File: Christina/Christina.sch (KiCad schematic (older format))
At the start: 20 parts, among them K1 FINDER-32.21-x300, M1 Motor_DC, M2 Motor_DC, M3 Motor_DC, Q1 BD139, SW1 SW_Push, SW2 SW_Push, U1 74LS386, U2 L7805

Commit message: Braking PCB Rev1
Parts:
- C1, C2: footprint (none) -> Capacitors_SMD:C_0805_HandSoldering
- D1, D2: footprint LEDs:LED_0603_HandSoldering -> TerminalBlock:TerminalBlock_bornier-2_P5.08mm
- K1: footprint Relays_THT:Relay_SPST_Finder_32.21-x300 -> .pretty:SPSTRELAYPANASONIC
- M1, M2, M3, SW1, SW2: footprint TerminalBlocks_Phoenix:TerminalBlock_Phoenix_MKDS1.5-2pol -> TerminalBlock:TerminalBlock_bornier-2_P5.08mm
- Q1: footprint TO_SOT_Packages_THT:TO-126_Vertical -> TO_SOT_Packages_THT:TO-126_Horizontal
- R1, R2, R3, R4, R5, R6, R7: footprint (none) -> Resistors_SMD:R_0805_HandSoldering
- U1: footprint (none) -> .pretty:XORGATE
- U2: footprint (none) -> TO_SOT_Packages_THT:TO-126_Horizontal
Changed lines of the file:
@@
 LIBS:contrib
 LIBS:valves
+LIBS:Christina-cache
 EELAYER 25 0
 EELAYER END
@@
 F 0 "M1" H 2800 2450 50  0000 L CNN
 F 1 "Motor_DC" H 2800 2150 50  0000 L TNN
-F 2 "TerminalBlocks_Phoenix:TerminalBlock_Phoenix_MKDS1.5-2pol" H 2700 2260 50  0001 C CNN
+F 2 "TerminalBlock:TerminalBlock_bornier-2_P5.08mm" H 2700 2260 50  0001 C CNN
 F 3 "" H 2700 2260 50  0001 C CNN
 	1    2700 2350
@@
 F 0 "M2" H 5100 2450 50  0000 L CNN
 F 1 "Motor_DC" H 5100 2150 50  0000 L TNN
-F 2 "TerminalBlocks_Phoenix:TerminalBlock_Phoenix_MKDS1.5-2pol" H 5000 2260 50  0001 C CNN
+F 2 "TerminalBlock:TerminalBlock_bornier-2_P5.08mm" H 5000 2260 50  0001 C CNN
 F 3 "" H 5000 2260 50  0001 C CNN
 	1    5000 2350
@@
 F 0 "SW1" H 3350 1900 50  0000 L CNN
 F 1 "SW_Push" H 3300 1740 50  0000 C CNN
-F 2 "TerminalBlocks_Phoenix:TerminalBlock_Phoenix_MKDS1.5-2pol" H 3300 2000 50  0001 C CNN
+F 2 "TerminalBlock:TerminalBlock_bornier-2_P5.08mm" H 3300 2000 50  0001 C CNN
 F 3 "" H 3300 2000 50  0001 C CNN
 	1    3300 1800
@@
 F 0 "SW2" H 4200 1900 50  0000 L CNN
 F 1 "SW_Push" H 4150 1740 50  0000 C CNN
-F 2 "TerminalBlocks_Phoenix:TerminalBlock_Phoenix_MKDS1.5-2pol" H 4150 2000 50  0001 C CNN
+F 2 "TerminalBlock:TerminalBlock_bornier-2_P5.08mm" H 4150 2000 50  0001 C CNN
 F 3 "" H 4150 2000 50  0001 C CNN
 	1    4150 1800
@@
 F 0 "R1" V 2130 2300 50  0000 C CNN
 F 1 "R" V 2050 2300 50  0000 C CNN
-F 2 "" V 1980 2300 50  0001 C CNN
+F 2 "Resistors_SMD:R_0805_HandSoldering" V 1980 2300 50  0001 C CNN
 F 3 "" H 2050 2300 50  0001 C CNN
 	1    2050 2300
@@
 F 0 "D2" H 5850 2800 50  0000 C CNN
 F 1 "LED" H 5850 2600 50  0000 C CNN
-F 2 "LEDs:LED_0603_HandSoldering" H 5850 2700 50  0001 C CNN
+F 2 "TerminalBlock:TerminalBlock_bornier-2_P5.08mm" H 5850 2700 50  0001 C CNN
 F 3 "" H 5850 2700 50  0001 C CNN
 	1    5850 2700
@@
 F 0 "D1" H 2050 2850 50  0000 C CNN
 F 1 "LED" H 2050 2650 50  0000 C CNN
-F 2 "LEDs:LED_0603_HandSoldering" H 2050 2750 50  0001 C CNN
+F 2 "TerminalBlock:TerminalBlock_bornier-2_P5.08mm" H 2050 2750 50  0001 C CNN
 F 3 "" H 2050 2750 50  0001 C CNN
 	1    2050 2750
@@
 F 0 "R2" V 4730 3300 50  0000 C CNN
 F 1 "R" V 4650 3300 50  0000 C CNN
-F 2 "" V 4580 3300 50  0001 C CNN
+F 2 "Resistors_SMD:R_0805_HandSoldering" V 4580 3300 50  0001 C CNN
 F 3 "" H 4650 3300 50  0001 C CNN
 	1    4650 3300
@@
 F 0 "R3" V 4730 3900 50  0000 C CNN
 F 1 "R" V 4650 3900 50  0000 C CNN
-F 2 "" V 4580 3900 50  0001 C CNN
+F 2 "Resistors_SMD:R_0805_HandSoldering" V 4580 3900 50  0001 C CNN
 F 3 "" H 4650 3900 50  0001 C CNN
 	1    4650 3900
@@
 F 0 "R4" V 5430 3500 50  0000 C CNN
 F 1 "R" V 5350 3500 50  0000 C CNN
-F 2 "" V 5280 3500 50  0001 C CNN
+F 2 "Resistors_SMD:R_0805_HandSoldering" V 5280 3500 50  0001 C CNN
 F 3 "" H 5350 3500 50  0001 C CNN
 	1    5350 3500
@@
 F 0 "R5" V 5430 4200 50  0000 C CNN
 F 1 "R" V 5350 4200 50  0000 C CNN
-F 2 "" V 5280 4200 50  0001 C CNN
+F 2 "Resistors_SMD:R_0805_HandSoldering" V 5280 4200 50  0001 C CNN
 F 3 "" H 5350 4200 50  0001 C CNN
 	1    5350 4200
@@
 F 0 "U1" H 7000 3700 50  0000 C CNN
 F 1 "74LS386" H 7000 3600 50  0000 C CNN
-F 2 "" H 7000 3650 50  0001 C CNN
+F 2 ".pretty:XORGATE" H 7000 3650 50  0001 C CNN
 F 3 "" H 7000 3650 50  0001 C CNN
 	1    7000 3650
@@
 F 0 "R7" V 8130 3650 50  0000 C CNN
 F 1 "R" V 8050 3650 50  0000 C CNN
-F 2 "" V 7980 3650 50  0001 C CNN
+F 2 "Resistors_SMD:R_0805_HandSoldering" V 7980 3650 50  0001 C CNN
 F 3 "" H 8050 3650 50  0001 C CNN
 	1    8050 3650
@@
 F 0 "M3" H 10100 3550 50  0000 L CNN
 F 1 "Motor_DC" H 10100 3250 50  0000 L TNN
-F 2 "TerminalBlocks_Phoenix:TerminalBlock_Phoenix_MKDS1.5-2pol" H 10000 3360 50  0001 C CNN
+F 2 "TerminalBlock:TerminalBlock_bornier-2_P5.08mm" H 10000 3360 50  0001 C CNN
 F 3 "" H 10000 3360 50  0001 C CNN
 	1    10000 3450
@@
 F 0 "K1" H 9450 2700 50  0000 L CNN
 F 1 "FINDER-32.21-x300" H 9450 2600 50  0000 L CNN
-F 2 "Relays_THT:Relay_SPST_Finder_32.21-x300" H 10270 2520 50  0001 C CNN
+F 2 ".pretty:SPSTRELAYPANASONIC" H 10270 2520 50  0001 C CNN
 F 3 "" H 9000 2550 50  0001 C CNN
 	1    9000 2550
@@
 F 0 "Q1" H 8850 3725 50  0000 L CNN
 F 1 "BD139" H 8850 3650 50  0000 L CNN
-F 2 "TO_SOT_Packages_THT:TO-126_Vertical" H 8850 3575 50  0001 L CIN
+F 2 "TO_SOT_Packages_THT:TO-126_Horizontal" H 8850 3575 50  0001 L CIN
 F 3 "" H 8650 3650 50  0001 L CNN
 	1    8650 3650
@@
 F 0 "U2" H 7150 1775 50  0000 C CNN
 F 1 "L7805" H 7300 1775 50  0000 L CNN
-F 2 "" H 7325 1500 50  0001 L CIN
+F 2 "TO_SOT_Packages_THT:TO-126_Horizontal" H 7325 1500 50  0001 L CIN
 F 3 "" H 7300 1600 50  0001 C CNN
 	1    7300 1650
@@
 F 0 "C2" H 7825 2100 50  0000 L CNN
 F 1 "C" H 7825 1900 50  0000 L CNN
-F 2 "" H 7838 1850 50  0001 C CNN
+F 2 "Capacitors_SMD:C_0805_HandSoldering" H 7838 1850 50  0001 C CNN
 F 3 "" H 7800 2000 50  0001 C CNN
 	1    7800 2000
@@
 F 0 "C1" H 6825 2050 50  0000 L CNN
 F 1 "C" H 6825 1850 50  0000 L CNN
-F 2 "" H 6838 1800 50  0001 C CNN
+F 2 "Capacitors_SMD:C_0805_HandSoldering" H 6838 1800 50  0001 C CNN
 F 3 "" H 6800 1950 50  0001 C CNN
 	1    6800 1950
@@
 F 0 "R6" V 5930 2300 50  0000 C CNN
 F 1 "R" V 5850 2300 50  0000 C CNN
-F 2 "" V 5780 2300 50  0001 C CNN
+F 2 "Resistors_SMD:R_0805_HandSoldering" V 5780 2300 50  0001 C CNN
 F 3 "" H 5850 2300 50  0001 C CNN
 	1    5850 2300

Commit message: uploaded rerouted board
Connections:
- net GND: now also U2.2 (GND)
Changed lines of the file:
@@
 	1    0    0    -1
 $EndComp
-Text GLabel 8100 1650 0    60   Output ~ 0
+Text GLabel 8450 1650 0    60   Output ~ 0
 Vcc
 $Comp
@@
 Connection ~ 6800 1650
 Wire Wire Line
-	7600 1650 8100 1650
+	7600 1650 8450 1650
 Wire Wire Line
 	7800 1850 7800 1650
@@
 Wire Wire Line
 	8750 4200 8750 3850
+$Comp
+L GND #PWR?
+U 1 1 5AF1FF8F
+P 7300 2000
+F 0 "#PWR?" H 7300 1750 50  0001 C CNN
+F 1 "GND" H 7300 1850 50  0000 C CNN
+F 2 "" H 7300 2000 50  0001 C CNN
+F 3 "" H 7300 2000 50  0001 C CNN
+	1    7300 2000
+	1    0    0    -1
+$EndComp
+Wire Wire Line
+	7300 2000 7300 1950
 $EndSCHEMATC

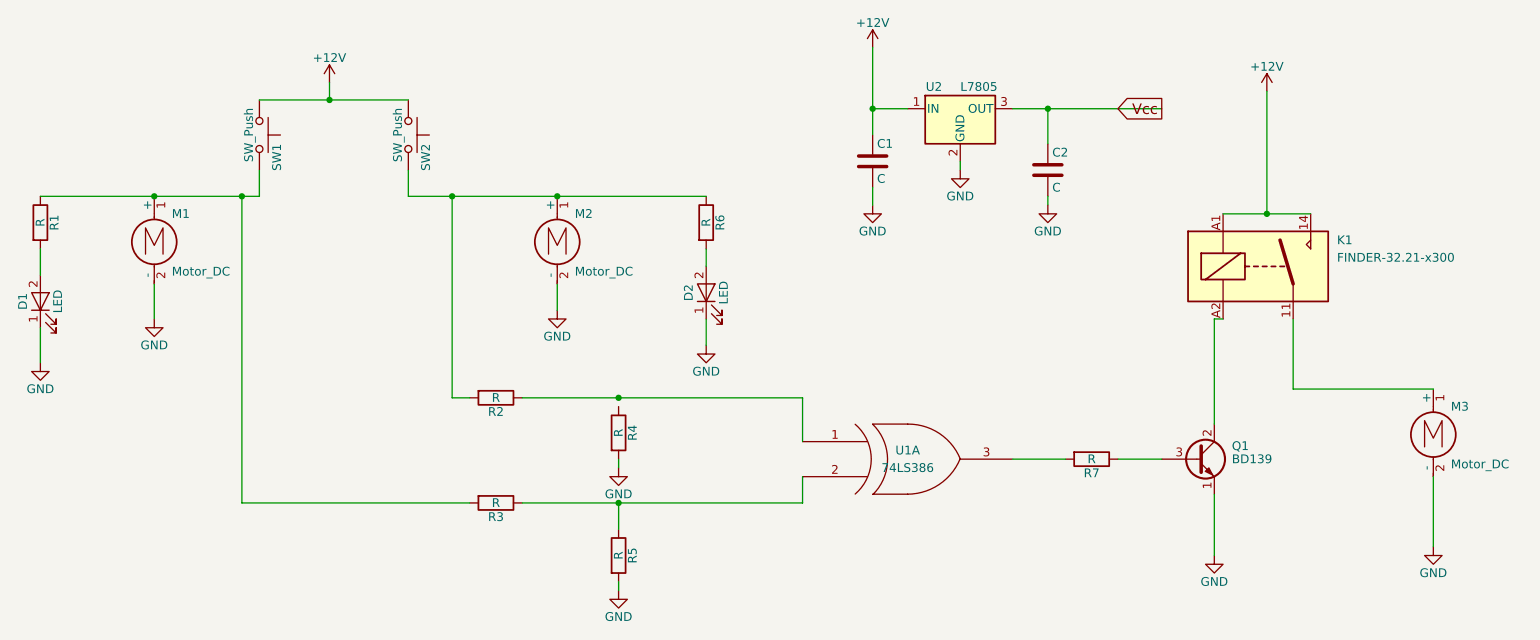
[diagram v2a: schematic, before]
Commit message: fixed routing, schematic issue
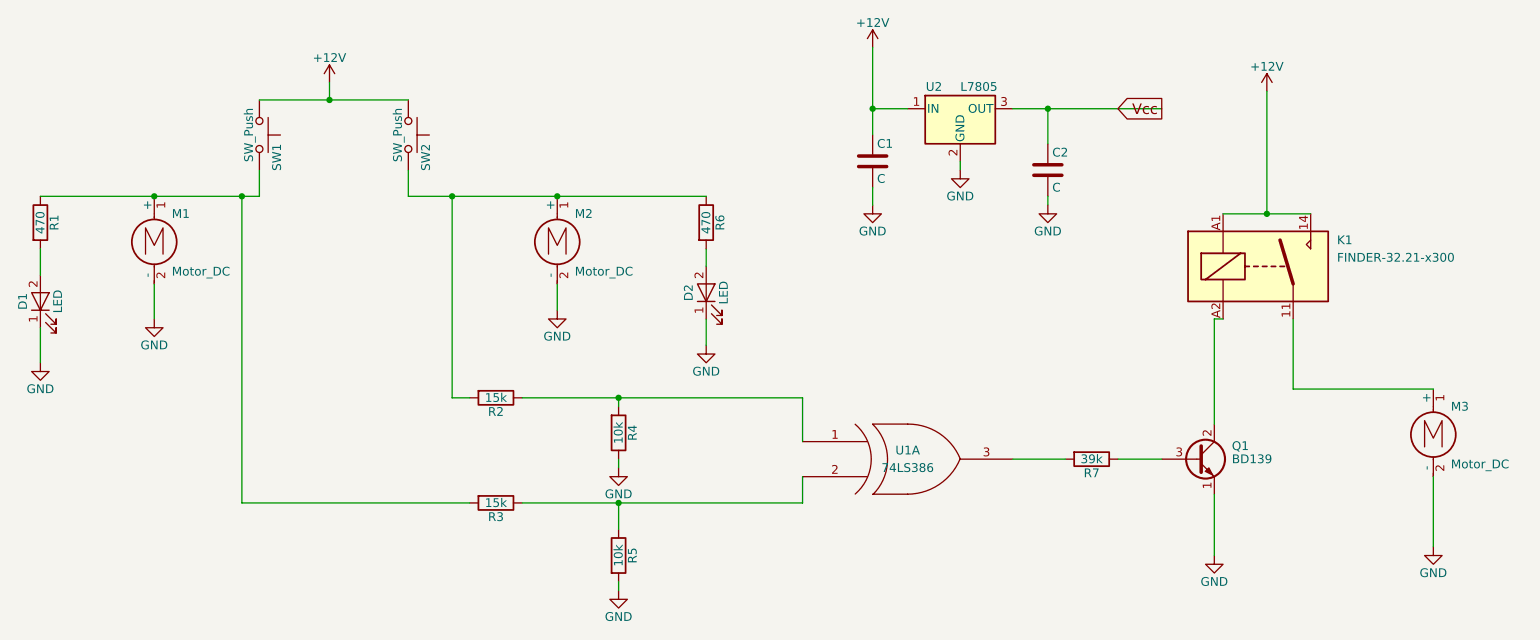
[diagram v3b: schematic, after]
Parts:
- R1, R6: value R -> 470
- R2, R3: value R -> 15k
- R4, R5: value R -> 10k
- R7: value R -> 39k
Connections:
- net GND: now also R4.1; no longer R4.2
- net at R2.1, U1.1: now also R4.2
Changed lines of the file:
@@
 P 2050 2300
 F 0 "R1" V 2130 2300 50  0000 C CNN
-F 1 "R" V 2050 2300 50  0000 C CNN
+F 1 "470" V 2050 2300 50  0000 C CNN
 F 2 "Resistors_SMD:R_0805_HandSoldering" V 1980 2300 50  0001 C CNN
 F 3 "" H 2050 2300 50  0001 C CNN
@@
 P 4650 3300
 F 0 "R2" V 4730 3300 50  0000 C CNN
-F 1 "R" V 4650 3300 50  0000 C CNN
+F 1 "15k" V 4650 3300 50  0000 C CNN
 F 2 "Resistors_SMD:R_0805_HandSoldering" V 4580 3300 50  0001 C CNN
 F 3 "" H 4650 3300 50  0001 C CNN
@@
 P 4650 3900
 F 0 "R3" V 4730 3900 50  0000 C CNN
-F 1 "R" V 4650 3900 50  0000 C CNN
+F 1 "15k" V 4650 3900 50  0000 C CNN
 F 2 "Resistors_SMD:R_0805_HandSoldering" V 4580 3900 50  0001 C CNN
 F 3 "" H 4650 3900 50  0001 C CNN
@@
 P 5350 3500
 F 0 "R4" V 5430 3500 50  0000 C CNN
-F 1 "R" V 5350 3500 50  0000 C CNN
+F 1 "10k" V 5350 3500 50  0000 C CNN
 F 2 "Resistors_SMD:R_0805_HandSoldering" V 5280 3500 50  0001 C CNN
 F 3 "" H 5350 3500 50  0001 C CNN
 	1    5350 3500
-	1    0    0    -1
+	1    0    0    1
 $EndComp
 $Comp
@@
 P 5350 4200
 F 0 "R5" V 5430 4200 50  0000 C CNN
-F 1 "R" V 5350 4200 50  0000 C CNN
+F 1 "10k" V 5350 4200 50  0000 C CNN
 F 2 "Resistors_SMD:R_0805_HandSoldering" V 5280 4200 50  0001 C CNN
 F 3 "" H 5350 4200 50  0001 C CNN
@@
 P 8050 3650
 F 0 "R7" V 8130 3650 50  0000 C CNN
-F 1 "R" V 8050 3650 50  0000 C CNN
+F 1 "39k" V 8050 3650 50  0000 C CNN
 F 2 "Resistors_SMD:R_0805_HandSoldering" V 7980 3650 50  0001 C CNN
 F 3 "" H 8050 3650 50  0001 C CNN
@@
 P 5850 2300
 F 0 "R6" V 5930 2300 50  0000 C CNN
-F 1 "R" V 5850 2300 50  0000 C CNN
+F 1 "470" V 5850 2300 50  0000 C CNN
 F 2 "Resistors_SMD:R_0805_HandSoldering" V 5780 2300 50  0001 C CNN
 F 3 "" H 5850 2300 50  0001 C CNN
@@
 Wire Wire Line
 	7300 2000 7300 1950
+Wire Wire Line
+	5350 3350 5350 3300
 $EndSCHEMATC
